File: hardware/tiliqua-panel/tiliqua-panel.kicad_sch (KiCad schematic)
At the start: 2 parts, among them J1 MountingHole_Pad, M1 MountingHole_Pad

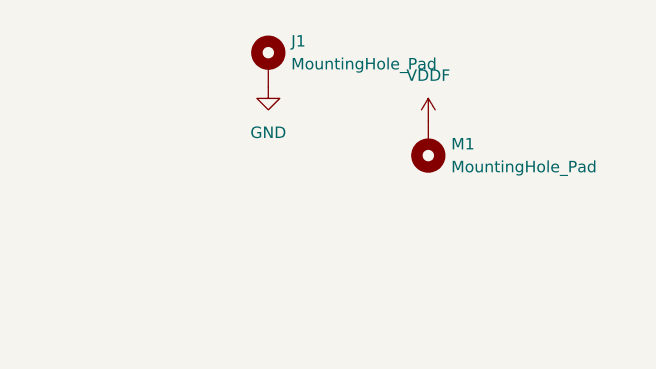
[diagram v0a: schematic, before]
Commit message: fix panel slots and move some things
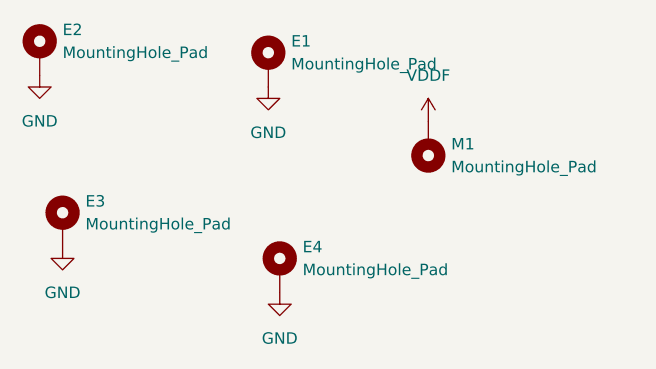
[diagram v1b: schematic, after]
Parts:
- added E2, E3, E4: MountingHole_Pad, symbol Mechanical:MountingHole_Pad
- renumbered J1 to E1
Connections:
- net GND: now also E2.1, E3.1, E4.1
